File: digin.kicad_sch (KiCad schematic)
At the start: 4 parts, among them J15 EPY.00.250.NTN, J16 EPY.00.250.NTN, J17 EPY.00.250.NTN, J18 EPY.00.250.NTN

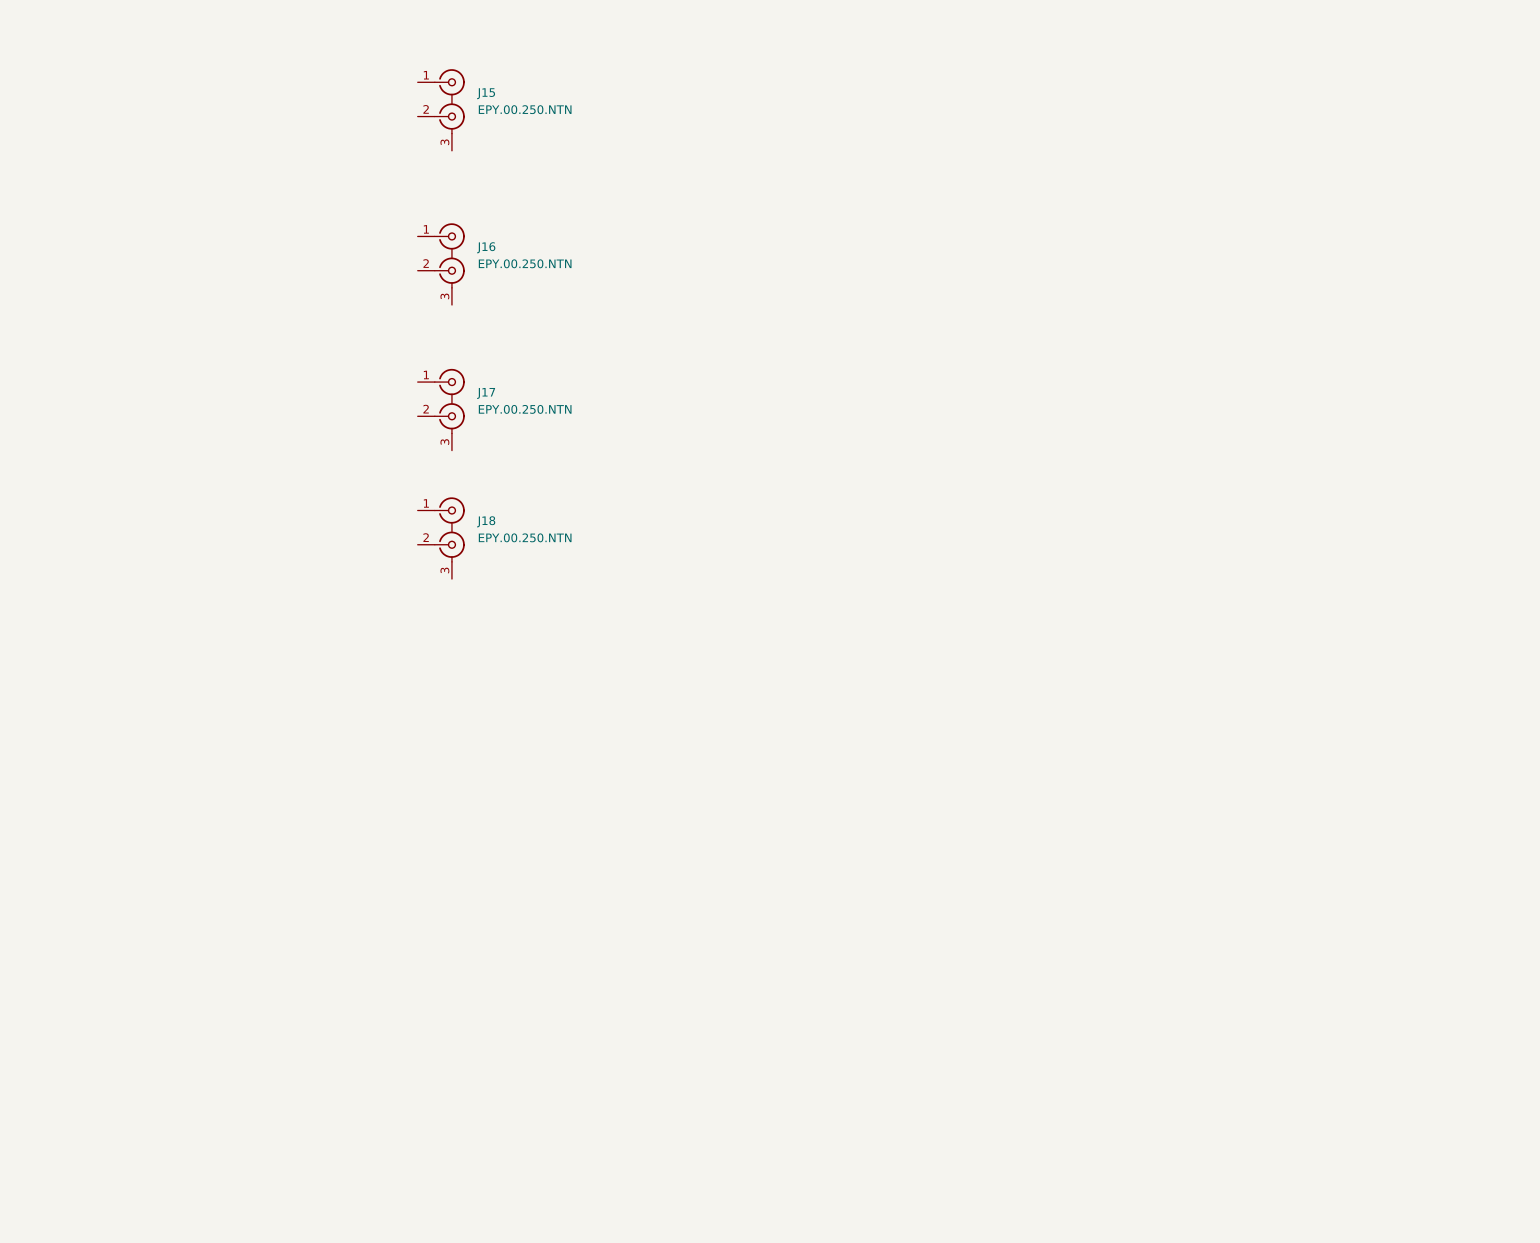
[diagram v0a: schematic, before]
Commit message: Start routing SFP
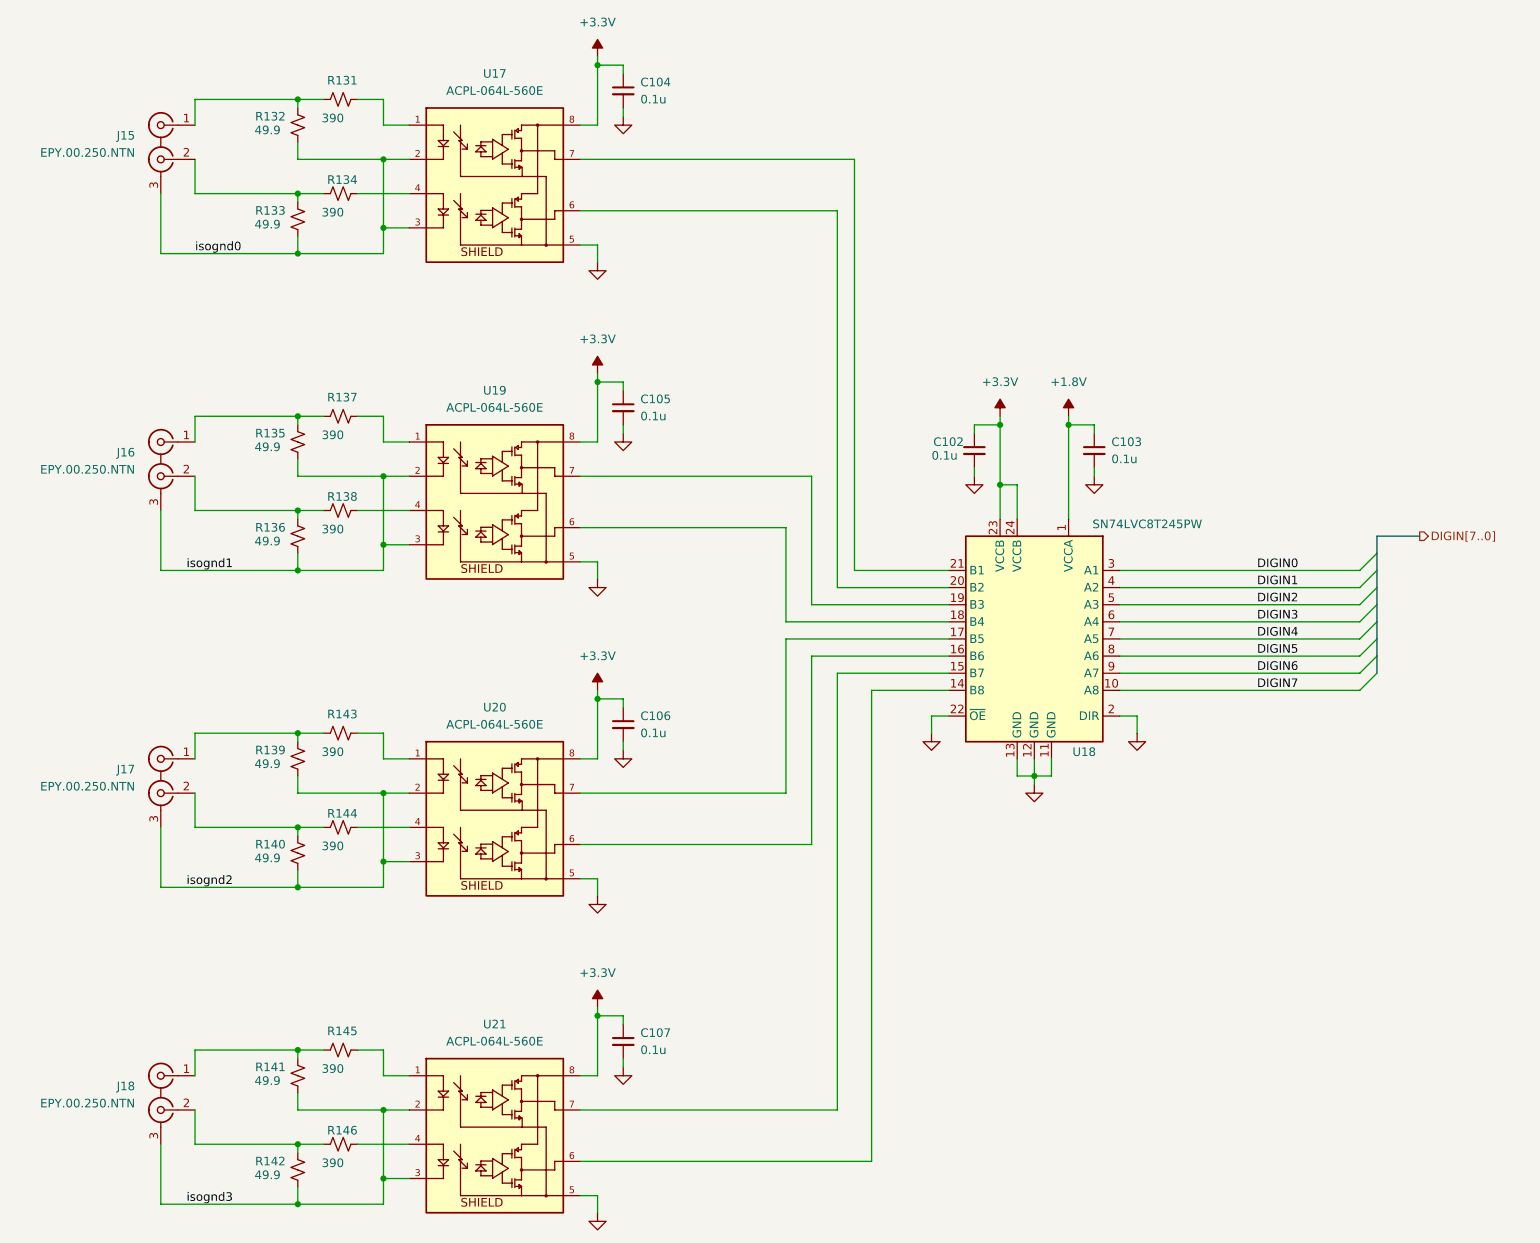
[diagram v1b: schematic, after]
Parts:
- added C102, C103, C104, C105, C106, C107: 0.1u, Capacitor_SMD:C_0603_1608Metric, symbol Device:C_Small
- added R131, R134, R137, R138, R143, R144, R145, R146: 390, Resistor_SMD:R_0603_1608Metric, symbol Device:R_Small_US
- added R132, R133, R135, R136, R139, R140, R141, R142: 49.9, Resistor_SMD:R_0603_1608Metric, symbol Device:R_Small_US
- added U17, U19, U20, U21: ACPL-064L-560E, My Footprints:OPTO_ACPL-064L-560E, symbol My Symbols:ACPL-064L-560E
- added U18: SN74LVC8T245PW, Package_SO:TSSOP-24_4.4x7.8mm_P0.65mm, symbol My Symbols:SN74LVC8T245PW
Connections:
- net at J16.1 (IN1): now also R135.2, R137.1
- net at J16.2 (IN2): now also R136.2, R138.1
- net isognd1: now reaches J16.3 (EXT)
- net isognd1: now also R135.1, R136.1, U19.2, U19.3
- net at J15.1 (IN1): now also R131.1, R132.2
- net at J15.2 (IN2): now also R133.2, R134.1
- net isognd0: now reaches J15.3 (EXT)
- net isognd0: now also R132.1, R133.1, U17.2, U17.3
- net at J17.1 (IN1): now also R139.2, R143.1
- net at J17.2 (IN2): now also R140.2, R144.1
- net isognd2: now reaches J17.3 (EXT)
- net isognd2: now also R139.1, R140.1, U20.2, U20.3
- net at J18.1 (IN1): now also R141.2, R145.1
- net at J18.2 (IN2): now also R142.2, R146.1
- net isognd3: now reaches J18.3 (EXT)
- net isognd3: now also R141.1, R142.1, U21.2, U21.3
- new net: R137.2, U19.1
- new net: R138.2, U19.4
- new net: U18.18 (B4), U19.6
- new net: U18.19 (B3), U19.7
- new net: R145.2, U21.1
- new net: R146.2, U21.4
- new net: U18.14 (B8), U21.6
- new net: U18.15 (B7), U21.7
- new net: R134.2, U17.4
- new net: R131.2, U17.1
- new net: U17.6, U18.20 (B2)
- new net: U17.7, U18.21 (B1)
- new net: R143.2, U20.1
- new net: R144.2, U20.4
- new net: U18.16 (B6), U20.6
- new net: U18.17 (B5), U20.7
- new net +1.8V: C103.1, U18.1 (VCCA)
- new net +3.3V: C102.1, C104.1, C105.1, C106.1, C107.1, U17.8, U18.23 (VCCB), U18.24 (VCCB), U19.8, U20.8, U21.8
- new net DIGIN0: U18.3 (A1)
- new net DIGIN1: U18.4 (A2)
- new net DIGIN2: U18.5 (A3)
- new net DIGIN3: U18.6 (A4)
- new net DIGIN4: U18.7 (A5)
- new net DIGIN5: U18.8 (A6)
- new net DIGIN6: U18.9 (A7)
- new net DIGIN7: U18.10 (A8)
- new net GND: C102.2, C103.2, C104.2, C105.2, C106.2, C107.2, U17.5, U18.11 (GND), U18.12 (GND), U18.13 (GND), U18.2 (DIR), U18.22 (~{OE}), U19.5, U20.5, U21.5
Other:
- moved on the sheet: J15
